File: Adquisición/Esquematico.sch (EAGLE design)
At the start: 8 parts, among them IC1 LM324N, M1 ELECTRET_MICROPHON-WM-62PC/62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

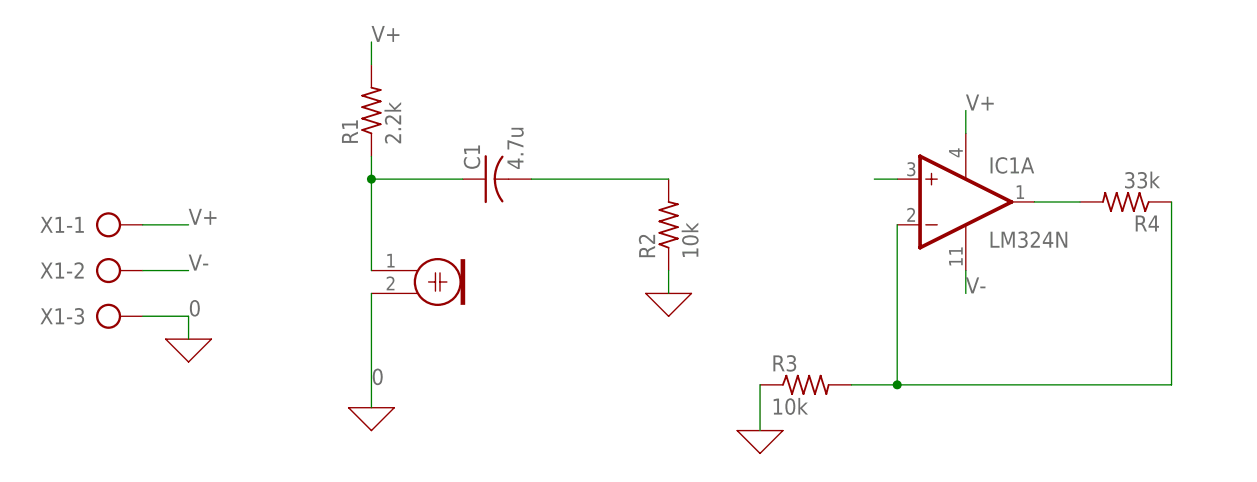
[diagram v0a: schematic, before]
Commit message: Se añade el puente H, y los gerber para las PCBs anteriores
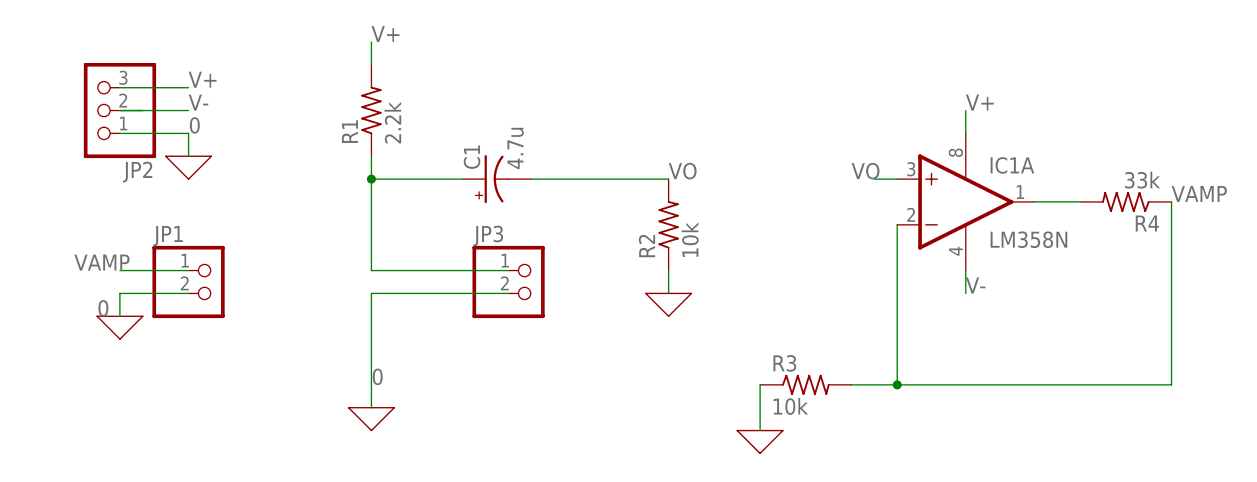
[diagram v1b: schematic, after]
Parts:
- removed M1: ELECTRET_MICROPHON-WM-62PC/62PK, microphon:ELECTRET_MICROPHON-WM-62PC/62PK
- removed X1: (no value), con-ptr500:AK300/3
- added JP1, JP3: (no value), pinhead:PINHD-1X2
- added JP2: (no value), pinhead:PINHD-1X3
- C1: device rcl:C-US025-024X044 -> rcl:CPOL-USE3.5-8
- IC1: value LM324N -> LM358N; device linear:LM324N -> linear:LM358N
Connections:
- removed net N$2: IC1A.+IN
- removed net N$3: C1.2, R2.2
- removed net N$4: IC1A.-IN, R3.2, R4.1
- new net VAMP: IC1A.-IN, JP1.1, R3.2, R4.1
- new net VO: C1.-, IC1A.+IN, R2.2
- net 0: now also JP1.2, JP2.1, JP3.2; no longer M1.2, X1-3.KL
- net N$1: now also C1.+, JP3.1; no longer C1.1, M1.1
- net V+: now also JP2.3; no longer X1-1.KL
- net V-: now also JP2.2; no longer X1-2.KL

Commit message: Se agregan pistas para los filtros y se crean los comparadores
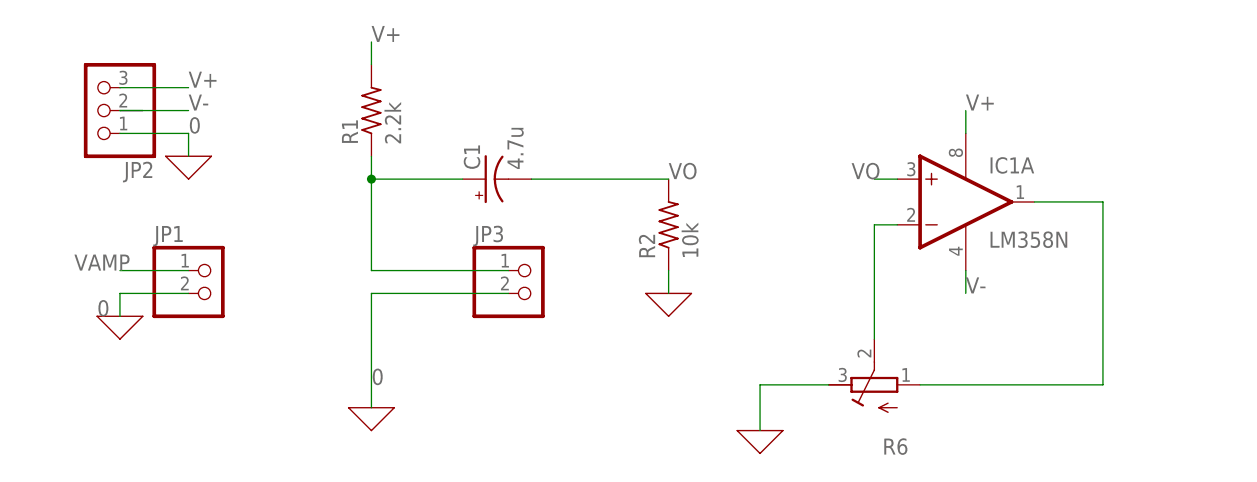
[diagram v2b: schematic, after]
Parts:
- removed R3: 10k, rcl:R-US_0207/10
- removed R4: 33k, rcl:R-US_0207/10
- added R6: (no value), rcl:R-TRIMM64W
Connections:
- removed net N$5: IC1A.OUT, R4.2
- new net N$2: IC1A.-IN, R6.S
- net 0: now also R6.E; no longer R3.1
- net VAMP: now also IC1A.OUT, R6.A; no longer IC1A.-IN, R3.2, R4.1
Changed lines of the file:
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@@
 <part name="IC1" library="linear" library_urn="urn:adsk.eagle:library:262" deviceset="LM358" device="N" package3d_urn="urn:adsk.eagle:package:16409/2"/>
 <part name="R2" library="rcl" library_urn="urn:adsk.eagle:library:334" deviceset="R-US_" device="0207/10" package3d_urn="urn:adsk.eagle:package:23491/2" value="10k"/>
-<part name="R4" library="rcl" library_urn="urn:adsk.eagle:library:334" deviceset="R-US_" device="0207/10" package3d_urn="urn:adsk.eagle:package:23491/2" value="33k"/>
-<part name="R3" library="rcl" library_urn="urn:adsk.eagle:library:334" deviceset="R-US_" device="0207/10" package3d_urn="urn:adsk.eagle:package:23491/2" value="10k"/>
 <part name="R1" library="rcl" library_urn="urn:adsk.eagle:library:334" deviceset="R-US_" device="0207/10" package3d_urn="urn:adsk.eagle:package:23491/2" value="2.2k"/>
 <part name="C1" library="rcl" library_urn="urn:adsk.eagle:library:334" deviceset="CPOL-US" device="E3.5-8" package3d_urn="urn:adsk.eagle:package:23360/2" value="4.7u"/>
@@
 <part name="JP2" library="pinhead" library_urn="urn:adsk.eagle:library:325" deviceset="PINHD-1X3" device="" package3d_urn="urn:adsk.eagle:package:22458/2"/>
 <part name="JP3" library="pinhead" library_urn="urn:adsk.eagle:library:325" deviceset="PINHD-1X2" device="" package3d_urn="urn:adsk.eagle:package:22435/2"/>
+<part name="R6" library="rcl" library_urn="urn:adsk.eagle:library:334" deviceset="R-TRIMM" device="64W" package3d_urn="urn:adsk.eagle:package:23748/1"/>
 </parts>
 <sheets>
@@
 <attribute name="NAME" x="79.7814" y="49.53" size="1.778" layer="95" rot="R90"/>
 <attribute name="VALUE" x="84.582" y="49.53" size="1.778" layer="96" rot="R90"/>
-</instance>
-<instance part="R4" gate="G$1" x="132.08" y="55.88" smashed="yes" rot="R180">
-<attribute name="NAME" x="135.89" y="54.3814" size="1.778" layer="95" rot="R180"/>
-<attribute name="VALUE" x="135.89" y="59.182" size="1.778" layer="96" rot="R180"/>
-</instance>
-<instance part="R3" gate="G$1" x="96.52" y="35.56" smashed="yes">
-<attribute name="NAME" x="92.71" y="37.0586" size="1.778" layer="95"/>
-<attribute name="VALUE" x="92.71" y="32.258" size="1.778" layer="96"/>
 </instance>
 <instance part="R1" gate="G$1" x="48.26" y="66.04" smashed="yes" rot="R90">
@@
 <attribute name="NAME" x="59.69" y="51.435" size="1.778" layer="95"/>
 <attribute name="VALUE" x="59.69" y="40.64" size="1.778" layer="96"/>
+</instance>
+<instance part="R6" gate="G$1" x="104.14" y="35.56" smashed="yes" rot="R90">
+<attribute name="NAME" x="107.95" y="29.591" size="1.778" layer="95" rot="R180"/>
+<attribute name="VALUE" x="107.95" y="31.75" size="1.778" layer="96" rot="R180"/>
 </instance>
 </instances>
@@
 <net name="VAMP" class="0">
 <segment>
-<pinref part="IC1" gate="A" pin="-IN"/>
-<wire x1="106.68" y1="53.34" x2="106.68" y2="35.56" width="0.1524" layer="91"/>
-<pinref part="R3" gate="G$1" pin="2"/>
-<wire x1="106.68" y1="35.56" x2="101.6" y2="35.56" width="0.1524" layer="91"/>
-<pinref part="R4" gate="G$1" pin="1"/>
-<wire x1="137.16" y1="55.88" x2="137.16" y2="35.56" width="0.1524" layer="91"/>
-<wire x1="137.16" y1="35.56" x2="106.68" y2="35.56" width="0.1524" layer="91"/>
-<junction x="106.68" y="35.56"/>
-<label x="137.16" y="55.88" size="1.778" layer="95"/>
-</segment>
-<segment>
 <pinref part="JP1" gate="G$1" pin="1"/>
 <wire x1="27.94" y1="48.26" x2="20.32" y2="48.26" width="0.1524" layer="91"/>
 <label x="15.24" y="48.26" size="1.778" layer="95"/>
 </segment>
-</net>
-<net name="N$5" class="0">
 <segment>
 <pinref part="IC1" gate="A" pin="OUT"/>
-<pinref part="R4" gate="G$1" pin="2"/>
-<wire x1="121.92" y1="55.88" x2="127" y2="55.88" width="0.1524" layer="91"/>
+<wire x1="121.92" y1="55.88" x2="129.54" y2="55.88" width="0.1524" layer="91"/>
+<pinref part="R6" gate="G$1" pin="A"/>
+<wire x1="129.54" y1="55.88" x2="129.54" y2="35.56" width="0.1524" layer="91"/>
+<wire x1="129.54" y1="35.56" x2="109.22" y2="35.56" width="0.1524" layer="91"/>
 </segment>
 </net>
@@
 </segment>
 <segment>
-<pinref part="R3" gate="G$1" pin="1"/>
 <pinref part="X_2" gate="G$1" pin="0"/>
 <wire x1="91.44" y1="35.56" x2="91.44" y2="30.48" width="0.1524" layer="91"/>
+<pinref part="R6" gate="G$1" pin="E"/>
+<wire x1="91.44" y1="35.56" x2="99.06" y2="35.56" width="0.1524" layer="91"/>
 </segment>
 <segment>
@@
 </segment>
 </net>
+<net name="N$2" class="0">
+<segment>
+<pinref part="IC1" gate="A" pin="-IN"/>
+<pinref part="R6" gate="G$1" pin="S"/>
+<wire x1="106.68" y1="53.34" x2="104.14" y2="53.34" width="0.1524" layer="91"/>
+<wire x1="104.14" y1="53.34" x2="104.14" y2="40.64" width="0.1524" layer="91"/>
+</segment>
+</net>
